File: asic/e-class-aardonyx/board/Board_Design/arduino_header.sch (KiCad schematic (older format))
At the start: 35 parts, among them J10 Conn_1x3_M, J14 Conn_1x4, J17 Conn_1x8, J18 Conn_1x3_M, J2 Conn_1x6, J3 Conn_1x10_F, J4 Conn_1x8_F, J5 Conn_1x8_F, J6 Conn_1x6_F, J7 Conn_1x3_M, J9 Conn_1x6, U1 LSF0108PWR, U4 LSF0108PWR, U6 ADC128S102CIMTX/NOPB, U8 IS25LP256x-xM, U9 CAT24M01WI-GT3

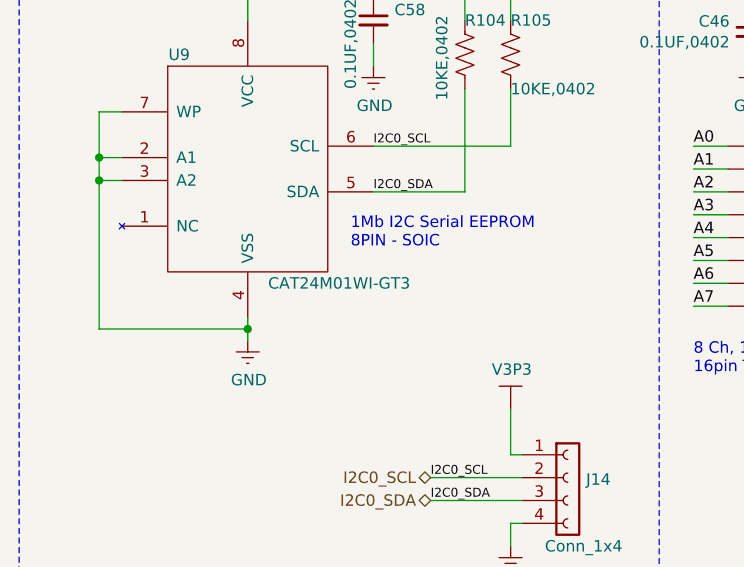
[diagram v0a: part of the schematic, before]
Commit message: Updating footprints
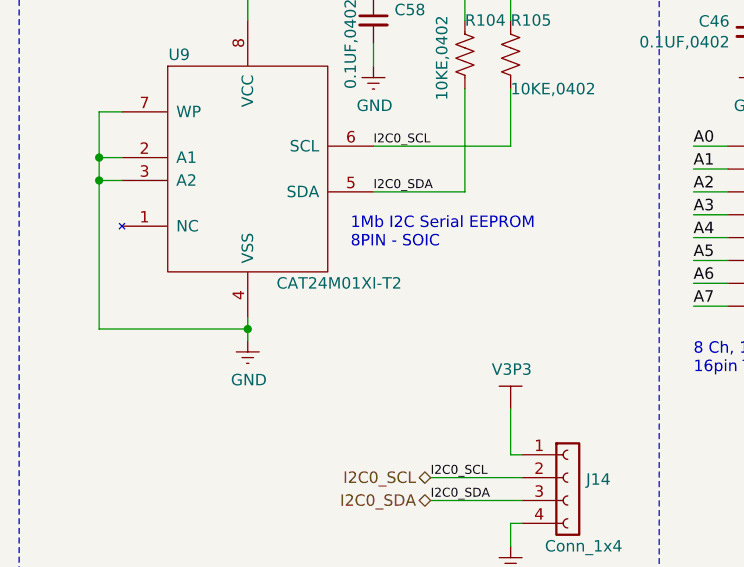
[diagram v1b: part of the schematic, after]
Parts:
- U9: value CAT24M01WI-GT3 -> CAT24M01XI-T2
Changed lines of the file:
@@
 P 1500 5650
 F 0 "U9" H 1200 6150 50  0000 C CNN
-F 1 "CAT24M01WI-GT3" H 1900 5150 50  0000 C CNN
+F 1 "CAT24M01XI-T2" H 1900 5150 50  0000 C CNN
 F 2 "Package_SO:SOIC-8_5.23x5.23mm_P1.27mm" H 1500 5650 50  0001 C CNN
 F 3 "https://www.digikey.in/product-detail/en/on-semiconductor/CAT24M01WI-GT3/CAT24M01WI-GT3OSCT-ND/2698362" H 1500 5650 50  0001 C CNN
